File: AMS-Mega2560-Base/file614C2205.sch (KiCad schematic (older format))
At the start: 4 parts, among them IC16 CD74HC4050ME4, IC17 CD74HC4050ME4, J22 2201778-1

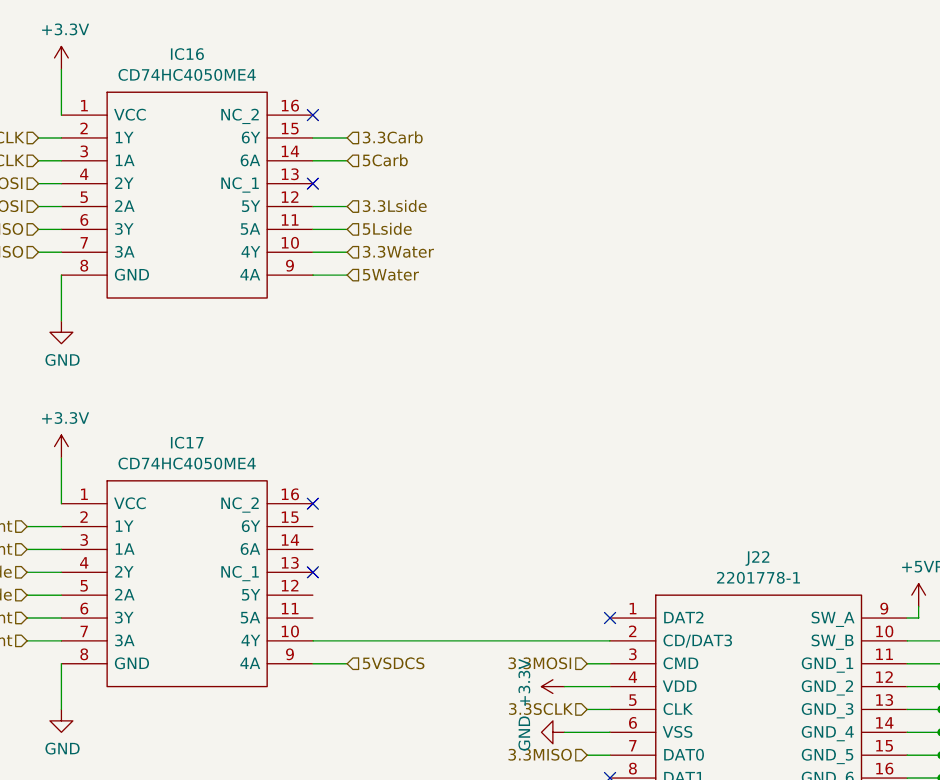
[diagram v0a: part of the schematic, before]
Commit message: rearranging some of the hw design before i rename the repo.
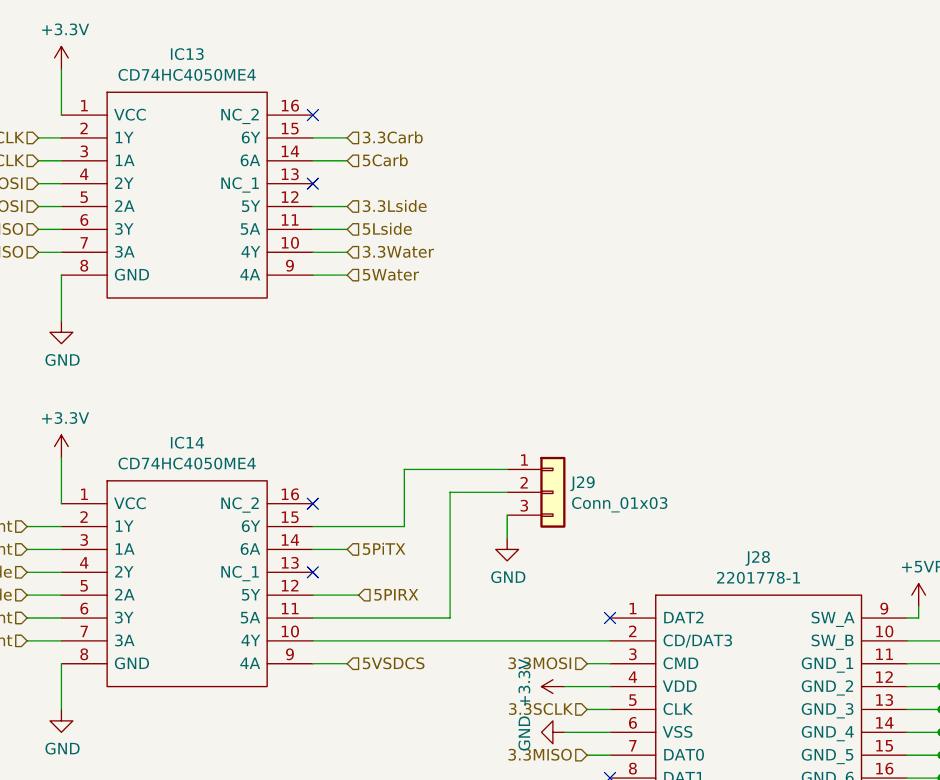
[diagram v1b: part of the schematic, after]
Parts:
- added J29: Conn_01x03, Connector_PinSocket_2.54mm:PinSocket_1x03_P2.54mm_Vertical, symbol Connector_Generic:Conn_01x03
- renumbered IC16 to IC13, IC17 to IC14, J22 to J28
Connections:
- net GND: now also J29.3 (Pin_3)
- net at IC14.11 (5A): now also J29.2 (Pin_2)
- net 5PIRX: now reaches IC14.12 (5Y)
- net 5PiTX: now reaches IC14.14 (6A)
- net at IC14.15 (6Y): now also J29.1 (Pin_1)
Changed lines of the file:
@@
 $Descr A4 11693 8268
 encoding utf-8
-Sheet 11 13
+Sheet 10 14
 Title ""
 Date ""
@@
 P 2100 2350
 AR Path="/614C7E9E" Ref="IC?"  Part="1"
-AR Path="/614C2206/614C7E9E" Ref="IC16"  Part="1"
-F 0 "IC16" H 2650 2615 50  0000 C CNN
+AR Path="/614C2206/614C7E9E" Ref="IC13"  Part="1"
+F 0 "IC13" H 2650 2615 50  0000 C CNN
 F 1 "CD74HC4050ME4" H 2650 2524 50  0000 C CNN
 F 2 "SamacSys_Parts:SOIC127P600X175-16N" H 3050 2450 50  0001 L CNN
@@
 NoConn ~ 3200 2650
 $Comp
-L power:+3.3V #PWR075
+L power:+3.3V #PWR081
 U 1 1 614C8EA1
 P 2100 2150
-F 0 "#PWR075" H 2100 2000 50  0001 C CNN
+F 0 "#PWR081" H 2100 2000 50  0001 C CNN
 F 1 "+3.3V" H 2115 2323 50  0000 C CNN
 F 2 "" H 2100 2150 50  0001 C CNN
@@
 $EndComp
 $Comp
-L power:GND #PWR076
+L power:GND #PWR082
 U 1 1 614C931C
 P 2100 3250
-F 0 "#PWR076" H 2100 3000 50  0001 C CNN
+F 0 "#PWR082" H 2100 3000 50  0001 C CNN
 F 1 "GND" H 2105 3077 50  0000 C CNN
 F 2 "" H 2100 3250 50  0001 C CNN
@@
 P 2100 4050
 AR Path="/614CD52C" Ref="IC?"  Part="1"
-AR Path="/614C2206/614CD52C" Ref="IC17"  Part="1"
-F 0 "IC17" H 2650 4315 50  0000 C CNN
+AR Path="/614C2206/614CD52C" Ref="IC14"  Part="1"
+F 0 "IC14" H 2650 4315 50  0000 C CNN
 F 1 "CD74HC4050ME4" H 2650 4224 50  0000 C CNN
 F 2 "SamacSys_Parts:SOIC127P600X175-16N" H 3050 4150 50  0001 L CNN
@@
 NoConn ~ 3200 4350
 $Comp
-L power:+3.3V #PWR077
+L power:+3.3V #PWR083
 U 1 1 614CD534
 P 2100 3850
-F 0 "#PWR077" H 2100 3700 50  0001 C CNN
+F 0 "#PWR083" H 2100 3700 50  0001 C CNN
 F 1 "+3.3V" H 2115 4023 50  0000 C CNN
 F 2 "" H 2100 3850 50  0001 C CNN
@@
 $EndComp
 $Comp
-L power:GND #PWR078
+L power:GND #PWR084
 U 1 1 614CD53A
 P 2100 4950
-F 0 "#PWR078" H 2100 4700 50  0001 C CNN
+F 0 "#PWR084" H 2100 4700 50  0001 C CNN
 F 1 "GND" H 2105 4777 50  0000 C CNN
 F 2 "" H 2100 4950 50  0001 C CNN
@@
 	3350 3050 3200 3050
 $Comp
-L SamacSys_Parts:2201778-1 J22
+L SamacSys_Parts:2201778-1 J28
 U 1 1 6158DF4E
 P 4500 4550
-F 0 "J22" H 5150 4815 50  0000 C CNN
+F 0 "J28" H 5150 4815 50  0000 C CNN
 F 1 "2201778-1" H 5150 4724 50  0000 C CNN
 F 2 "SamacSys_Parts:22017781" H 5650 4650 50  0001 L CNN
@@
 $EndComp
 $Comp
-L power:GND #PWR082
+L power:GND #PWR088
 U 1 1 6158F461
 P 5950 5450
-F 0 "#PWR082" H 5950 5200 50  0001 C CNN
+F 0 "#PWR088" H 5950 5200 50  0001 C CNN
 F 1 "GND" H 5955 5277 50  0000 C CNN
 F 2 "" H 5950 5450 50  0001 C CNN
@@
 	4500 4950 4400 4950
 $Comp
-L power:+3.3V #PWR079
+L power:+3.3V #PWR085
 U 1 1 615961B6
 P 4300 4850
-F 0 "#PWR079" H 4300 4700 50  0001 C CNN
+F 0 "#PWR085" H 4300 4700 50  0001 C CNN
 F 1 "+3.3V" H 4315 5023 50  0000 C CNN
 F 2 "" H 4300 4850 50  0001 C CNN
@@
 	3350 4750 3200 4750
 $Comp
-L power:GND #PWR083
+L power:GND #PWR089
 U 1 1 61599398
 P 6150 5200
-F 0 "#PWR083" H 6150 4950 50  0001 C CNN
+F 0 "#PWR089" H 6150 4950 50  0001 C CNN
 F 1 "GND" H 6155 5027 50  0000 C CNN
 F 2 "" H 6150 5200 50  0001 C CNN
@@
 	3200 4650 4500 4650
 $Comp
-L power:GND #PWR080
+L power:GND #PWR086
 U 1 1 615C4730
 P 4300 5050
-F 0 "#PWR080" H 4300 4800 50  0001 C CNN
+F 0 "#PWR086" H 4300 4800 50  0001 C CNN
 F 1 "GND" H 4305 4877 50  0000 C CNN
 F 2 "" H 4300 5050 50  0001 C CNN
@@
 P 5850 4500
 AR Path="/61493C0E/6171D932" Ref="#PWR?"  Part="1"
-AR Path="/614C2206/6171D932" Ref="#PWR081"  Part="1"
-F 0 "#PWR081" H 5850 4350 50  0001 C CNN
+AR Path="/614C2206/6171D932" Ref="#PWR087"  Part="1"
+F 0 "#PWR087" H 5850 4350 50  0001 C CNN
 F 1 "+5VP" H 5865 4673 50  0000 C CNN
 F 2 "" H 5850 4500 50  0001 C CNN
@@
 	1    0    0    -1
 $EndComp
+Text HLabel 3350 4250 2    50   Input ~ 0
+5PiTX
+Text HLabel 3400 4450 2    50   Input ~ 0
+5PIRX
+Wire Wire Line
+	3350 4250 3200 4250
+Wire Wire Line
+	3400 4450 3200 4450
+$Comp
+L Connector_Generic:Conn_01x03 J29
+U 1 1 61867B8B
+P 4250 4000
+F 0 "J29" H 4330 4042 50  0000 L CNN
+F 1 "Conn_01x03" H 4330 3951 50  0000 L CNN
+F 2 "Connector_PinSocket_2.54mm:PinSocket_1x03_P2.54mm_Vertical" H 4250 4000 50  0001 C CNN
+F 3 "~" H 4250 4000 50  0001 C CNN
+	1    4250 4000
+	1    0    0    -1
+$EndComp
+Wire Wire Line
+	3200 4150 3600 4150
+Wire Wire Line
+	3600 4150 3600 3900
+Wire Wire Line
+	3600 3900 4050 3900
+Wire Wire Line
+	3200 4550 3800 4550
+Wire Wire Line
+	3800 4550 3800 4000
+Wire Wire Line
+	3800 4000 4050 4000
+$Comp
+L power:GND #PWR0124
+U 1 1 6186A7BF
+P 4050 4200
+F 0 "#PWR0124" H 4050 3950 50  0001 C CNN
+F 1 "GND" H 4055 4027 50  0000 C CNN
+F 2 "" H 4050 4200 50  0001 C CNN
+F 3 "" H 4050 4200 50  0001 C CNN
+	1    4050 4200
+	1    0    0    -1
+$EndComp
+Wire Wire Line
+	4050 4200 4050 4100
 $EndSCHEMATC

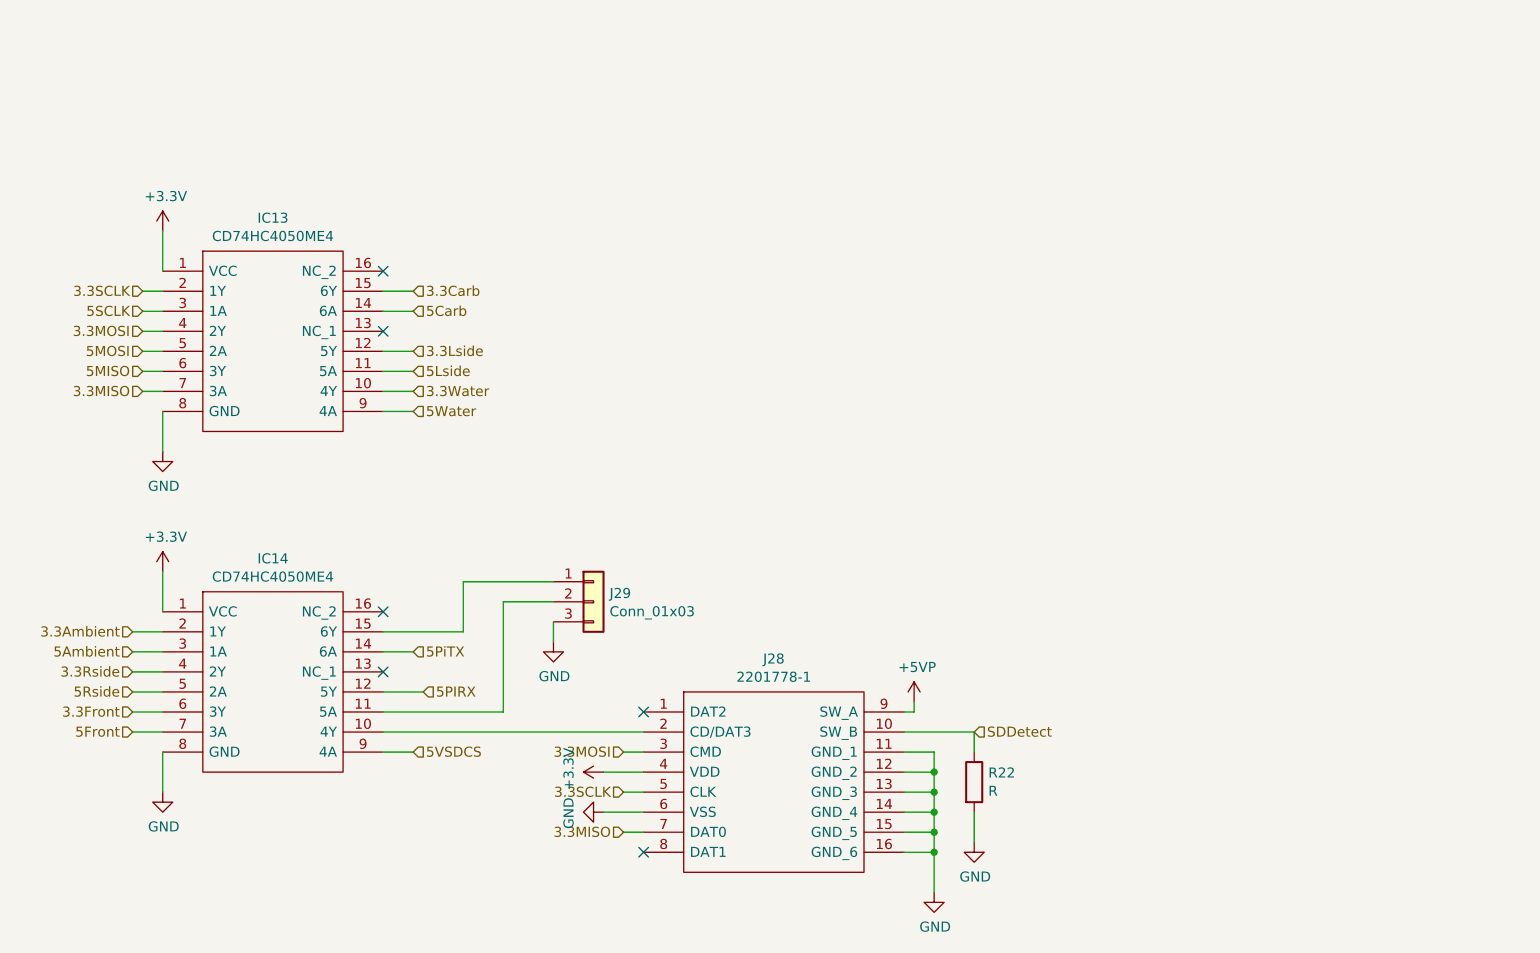
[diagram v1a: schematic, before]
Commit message: upgrading this to 6.0 and moving the vacuum sensors to a daughter board project.
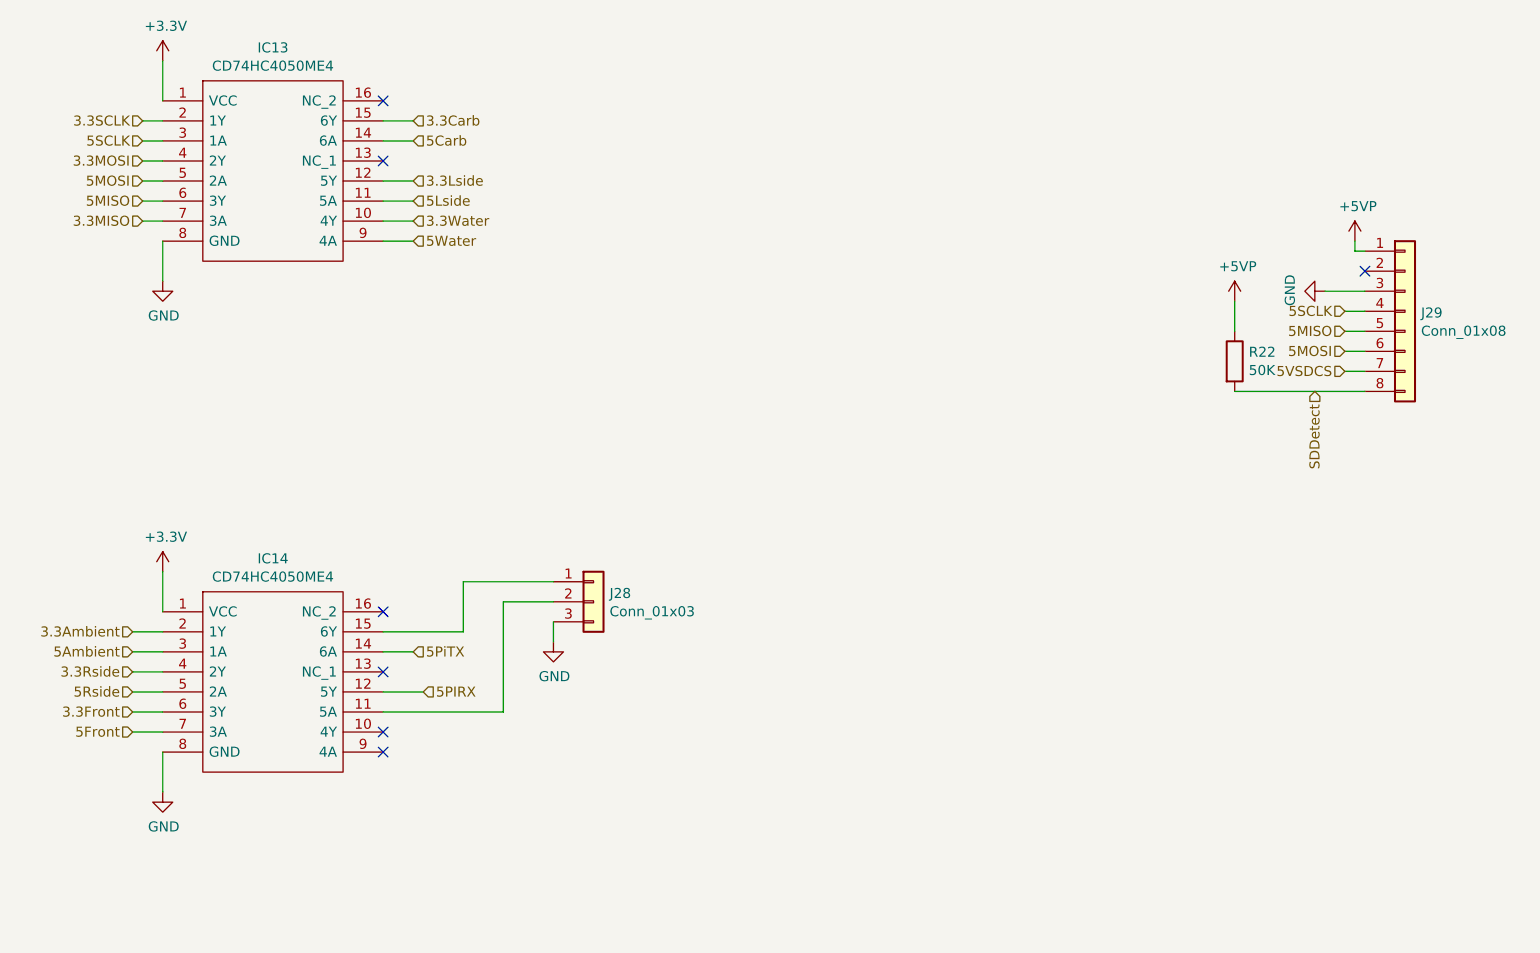
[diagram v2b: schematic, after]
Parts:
- removed J28: 2201778-1, SamacSys_Parts:22017781, symbol SamacSys_Parts:2201778-1
- added J29: Conn_01x08, Connector_PinSocket_2.54mm:PinSocket_1x08_P2.54mm_Horizontal, symbol Connector_Generic:Conn_01x08
- R22: value R -> 50K
- renumbered J29 to J28
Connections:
- net +5VP: now also R22.1, J29.1 (Pin_1)
- net 5MISO: now also J29.5 (Pin_5)
- net 5MOSI: now also J29.6 (Pin_6)
- net 5SCLK: now also J29.4 (Pin_4)
- net 5VSDCS: now also J29.7 (Pin_7); no longer IC14.9 (4A)
- net GND: now also J29.3 (Pin_3); no longer R22.2
- net SDDetect: now also R22.2, J29.8 (Pin_8); no longer R22.1
- no-connect marks 6 -> 7
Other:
- moved on the sheet: IC13, R22
